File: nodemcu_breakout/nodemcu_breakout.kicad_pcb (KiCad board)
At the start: 2 copper layers, 40.6 x 50.8 mm, 30 parts, among them J2 Conn_01x19, J3 Conn_01x19, Q1 2N7002, Q10 SSM3J332R, Q11 2N7002, Q12 SSM3J332R, Q2 SSM3J332R, Q3 2N7002, Q4 SSM3J332R, Q5 2N7002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

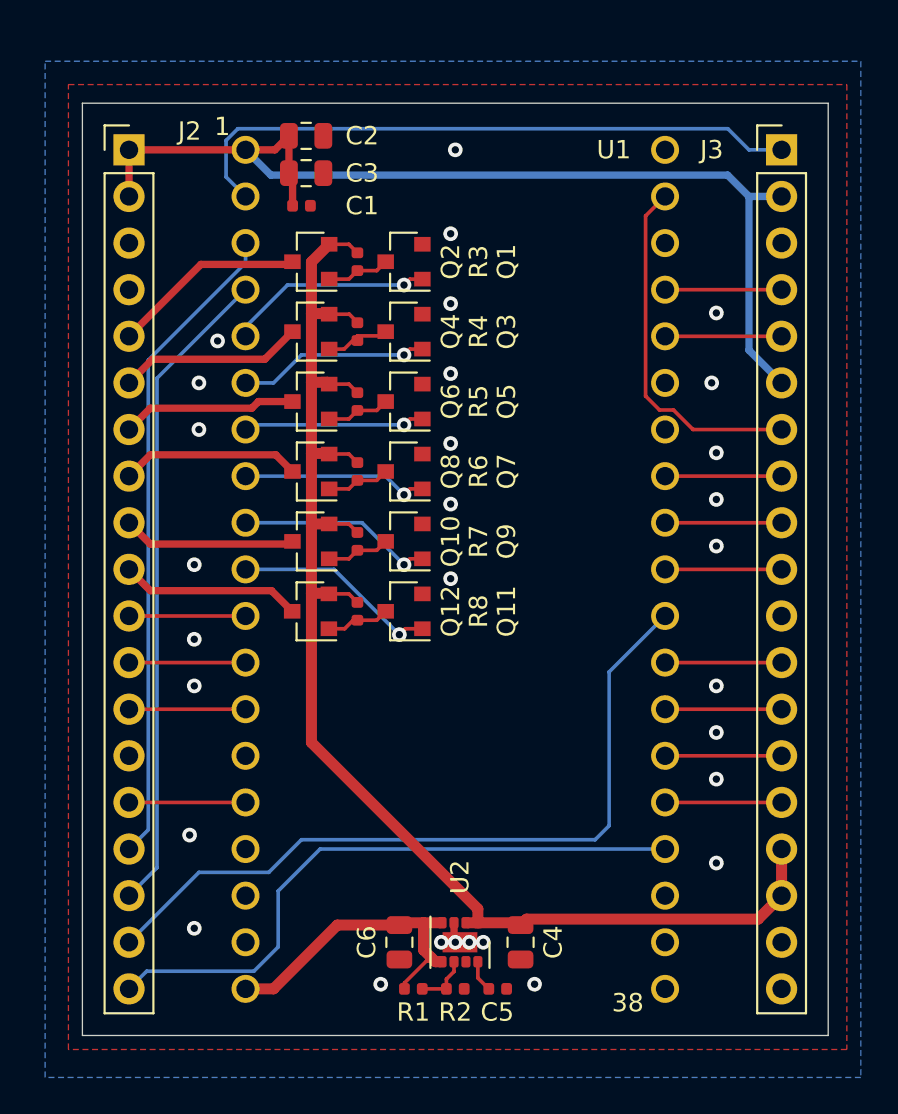
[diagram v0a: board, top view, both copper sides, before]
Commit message: v2, added nmos pwm out
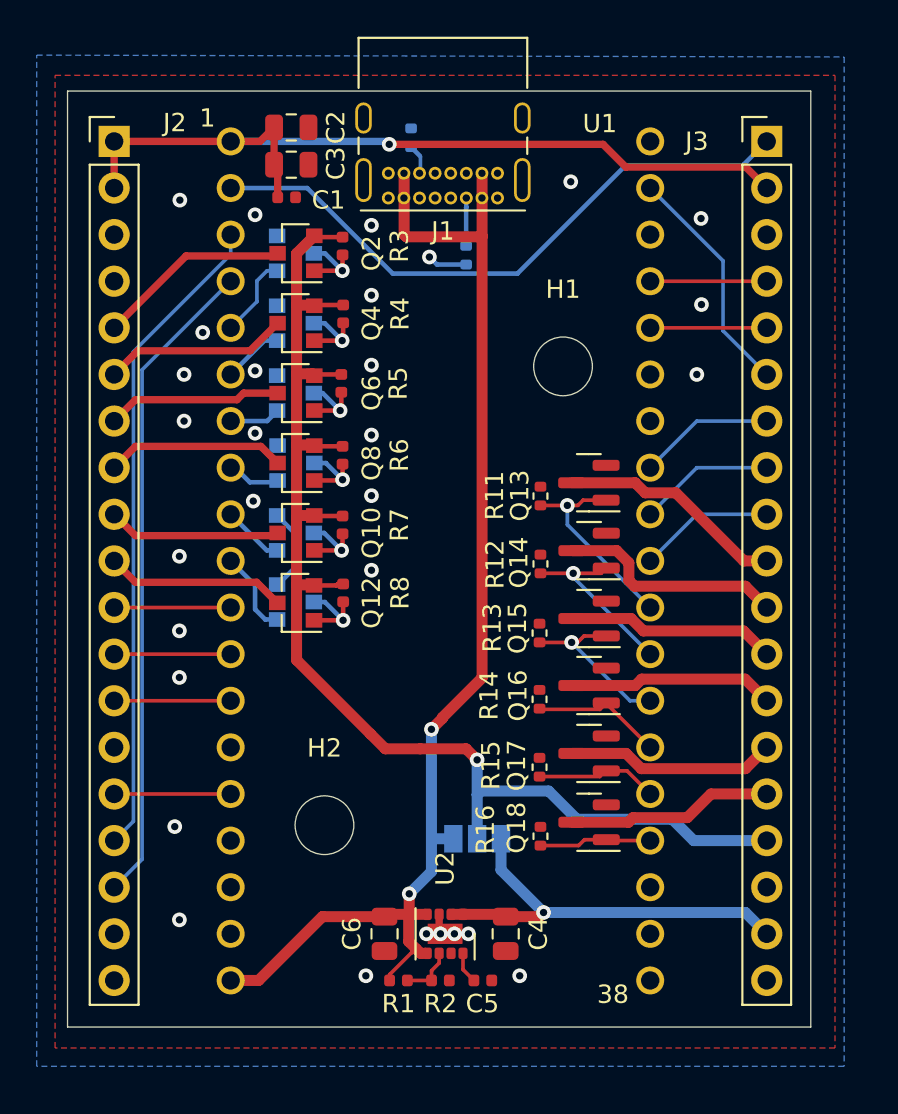
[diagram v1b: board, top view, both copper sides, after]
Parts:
- added H1: MountingHole, MountingHole:MountingHole_3.2mm_M3, F.Cu at (157.0, 88.0)
- added H2: MountingHole, MountingHole:MountingHole_3.2mm_M3, F.Cu at (144.0, 113.0)
- added J1: USB_C_Receptacle_USB2.0, Connector_USB:USB_C_Receptacle_GCT_USB4085, F.Cu at (153.4, 78.8)
- added JP1: SolderJumper_3_Open, Jumper:SolderJumper-3_P1.3mm_Open_Pad1.0x1.5mm, B.Cu at (152.3, 113.7)
- added Q13: SSM3K336R, Package_TO_SOT_SMD:SOT-23, F.Cu at (158.4, 94.3)
- added Q14: SSM3K336R, Package_TO_SOT_SMD:SOT-23, F.Cu at (158.4, 98.0)
- added Q15: SSM3K336R, Package_TO_SOT_SMD:SOT-23, F.Cu at (158.4, 101.7)
- added Q16: SSM3K336R, Package_TO_SOT_SMD:SOT-23, F.Cu at (158.4, 105.4)
- added Q17: SSM3K336R, Package_TO_SOT_SMD:SOT-23, F.Cu at (158.4, 109.1)
- added Q18: SSM3K336R, Package_TO_SOT_SMD:SOT-23, F.Cu at (158.4, 112.8)
- added R10: 5k1, Resistor_SMD:R_0402_1005Metric, B.Cu at (148.7, 75.5)
- added R11: 100k, Resistor_SMD:R_0402_1005Metric, F.Cu at (155.8, 95.1)
- added R12: 100k, Resistor_SMD:R_0402_1005Metric, F.Cu at (155.8, 98.8)
- added R13: 100k, Resistor_SMD:R_0402_1005Metric, F.Cu at (155.7, 102.5)
- added R14: 100k, Resistor_SMD:R_0402_1005Metric, F.Cu at (155.7, 106.1)
- added R15: 100k, Resistor_SMD:R_0402_1005Metric, F.Cu at (155.7, 109.8)
- added R16: 100k, Resistor_SMD:R_0402_1005Metric, F.Cu at (155.8, 113.6)
- added R9: 5k1, Resistor_SMD:R_0402_1005Metric, B.Cu at (151.7, 81.9)
- Q1, Q11, Q3, Q5, Q7, Q9: moved to B.Cu
- moved Q11 5.94 mm to (142.4, 100.8), turned to 0 degrees
- moved Q9 5.93 mm to (142.4, 97.1), turned to 0 degrees
- moved Q3 5.93 mm to (142.4, 85.6), turned to 0 degrees
- moved Q5 5.93 mm to (142.4, 89.5), turned to 0 degrees
- moved Q1 5.93 mm to (142.4, 81.8), turned to 0 degrees
- moved Q7 5.91 mm to (142.4, 93.3), turned to 0 degrees
- moved R5 1.32 mm to (144.9, 88.9)
- moved R8 1.27 mm to (145.0, 100.3)
- moved R4 1.24 mm to (145.0, 85.1)
- moved R7 1.21 mm to (145.0, 96.6)
- moved R6 1.20 mm to (145.0, 92.8)
- moved R3 1.18 mm to (145.0, 81.4)
- moved C1 0.93 mm to (141.9, 78.8)
- moved C2 0.93 mm to (142.2, 75.0)
- moved C5 0.93 mm to (152.6, 121.5)
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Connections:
- net /PWM_0_OUT renamed /PWM_H0_OUT
- net /PWM_1_OUT renamed /PWM_H1_OUT
- net /PWM_2_OUT renamed /PWM_H2_OUT
- net /PWM_3_OUT renamed /PWM_H3_OUT
- net /PWM_4_OUT renamed /PWM_H4_OUT
- net /PWM_5_OUT renamed /PWM_H5_OUT
- J2 pad 18: /P17 -> unconnected-(J2-Pad18)
- J2 pad 19: /P15 -> unconnected-(J2-Pad19)
- J3 pad 10: /spi_nSS -> /PWM_L0_OUT
- J3 pad 11: GND -> /PWM_L1_OUT
- J3 pad 12: /P16 -> /PWM_L2_OUT
- J3 pad 13: /P4 -> /PWM_L3_OUT
- J3 pad 14: /P0 -> /PWM_L4_OUT
- J3 pad 15: /P2 -> /PWM_L5_OUT
- J3 pad 16: +VDC -> /PWR_OUT
- J3 pad 17: +VDC -> GND
- J3 pad 18: GND -> +VDC
- J3 pad 6: +3V3 -> /spi_mosi
- J3 pad 7: /spi_mosi -> /spi_miso
- J3 pad 8: /spi_miso -> /spi_sck
- J3 pad 9: /spi_sck -> /spi_nSS
- Q10 pad 2: +VDC -> /PWR_OUT
- Q12 pad 2: +VDC -> /PWR_OUT
- Q2 pad 2: +VDC -> /PWR_OUT
- Q4 pad 2: +VDC -> /PWR_OUT
- Q6 pad 2: +VDC -> /PWR_OUT
- Q8 pad 2: +VDC -> /PWR_OUT
- R3 pad 1: +VDC -> /PWR_OUT
- R4 pad 1: +VDC -> /PWR_OUT
- R5 pad 1: +VDC -> /PWR_OUT
- R6 pad 1: +VDC -> /PWR_OUT
- R7 pad 1: +VDC -> /PWR_OUT
- R8 pad 1: +VDC -> /PWR_OUT
- U1 pad 16: Net-(U1-Pad16) -> unconnected-(U1-Pad16)
- U1 pad 17: Net-(U1-Pad17) -> unconnected-(U1-Pad17)
- U1 pad 18: Net-(U1-Pad18) -> unconnected-(U1-Pad18)
- U1 pad 22: Net-(U1-Pad22) -> unconnected-(U1-Pad22)
- U1 pad 25: Net-(U1-Pad25) -> unconnected-(U1-Pad25)
- U1 pad 30: /P17 -> /PWM_6
- U1 pad 31: /P16 -> /PWM_7
- U1 pad 32: /P4 -> /PWM_8
- U1 pad 33: /P0 -> /PWM_9
- U1 pad 34: /P2 -> /PWM_10
- U1 pad 35: /P15 -> /PWM_11
- U1 pad 36: Net-(U1-Pad36) -> unconnected-(U1-Pad36)
- U1 pad 37: Net-(U1-Pad37) -> unconnected-(U1-Pad37)
- U1 pad 38: Net-(U1-Pad38) -> unconnected-(U1-Pad38)
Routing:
- net /PWR_OUT: track 0.00 -> 71.2 mm, vias 0 -> 1
- net +VDC: track 76.9 -> 22.7 mm, vias 0 -> 1
- net +5V: track 17.1 -> 68.0 mm, vias 0 -> 2
- net /P17: track 41.5 -> 0.00 mm
- net /P15: track 34.2 -> 0.00 mm
- net /PWM_L1_OUT: track 0.00 -> 12.5 mm
- net /PWM_L0_OUT: track 0.00 -> 12.4 mm
- net /PWM_L4_OUT: track 0.00 -> 11.4 mm
- net /PWM_L2_OUT: track 0.00 -> 11.4 mm
- net /PWM_L5_OUT: track 0.00 -> 11.3 mm
- net /PWM_L3_OUT: track 0.00 -> 11.3 mm
- net /PWM_6: track 0.00 -> 11.1 mm, vias 0 -> 1
- net +3V3: track 56.6 -> 45.7 mm, vias 0 -> 1
- net /PWM_7: track 0.00 -> 9.85 mm, vias 0 -> 1
- net /PWM_8: track 0.00 -> 9.38 mm, vias 0 -> 1
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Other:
- board size 40.6 x 50.8 mm -> 40.5 x 51 mm
- net class Default removed
- board text added: "NodeMCU ESP-32S Breakout v2 Manuel Seeböck"
- board text removed: "NodeMCU ESP-32S Breakout v1 Manuel Seeböck"
